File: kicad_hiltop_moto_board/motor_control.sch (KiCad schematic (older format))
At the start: 60 parts, among them Q1 CSD18540Q5B, Q2 CSD18540Q5B, Q3 CSD18540Q5B, Q4 CSD18540Q5B, Q5 CSD18540Q5B, Q6 CSD18540Q5B, Q7 CSD18540Q5B, Q8 CSD18540Q5B, U1 DRV8704

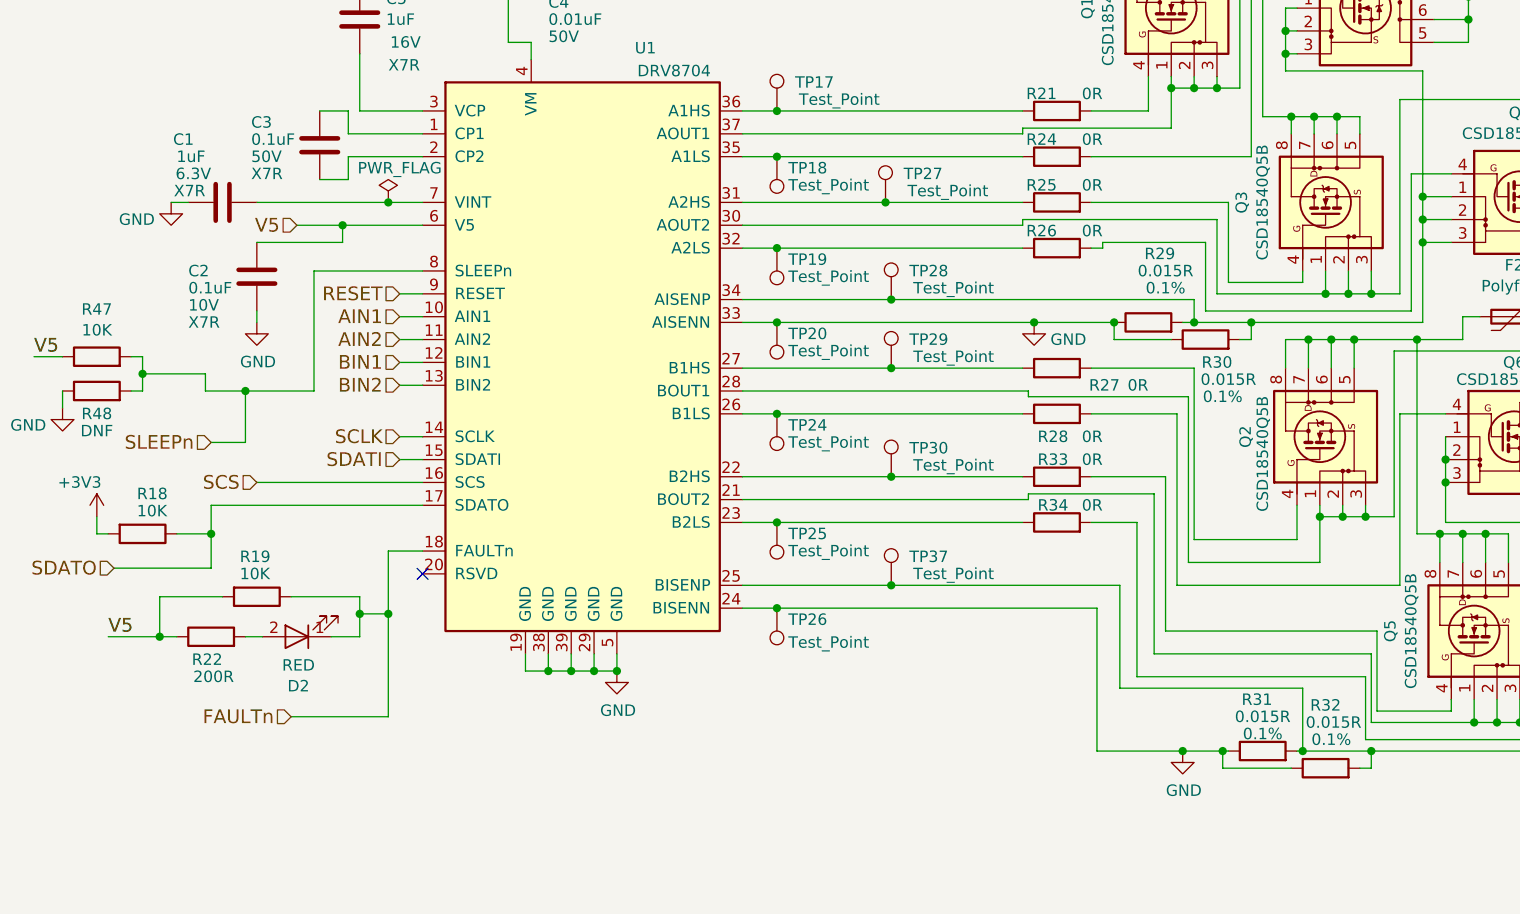
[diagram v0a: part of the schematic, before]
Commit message: added bom
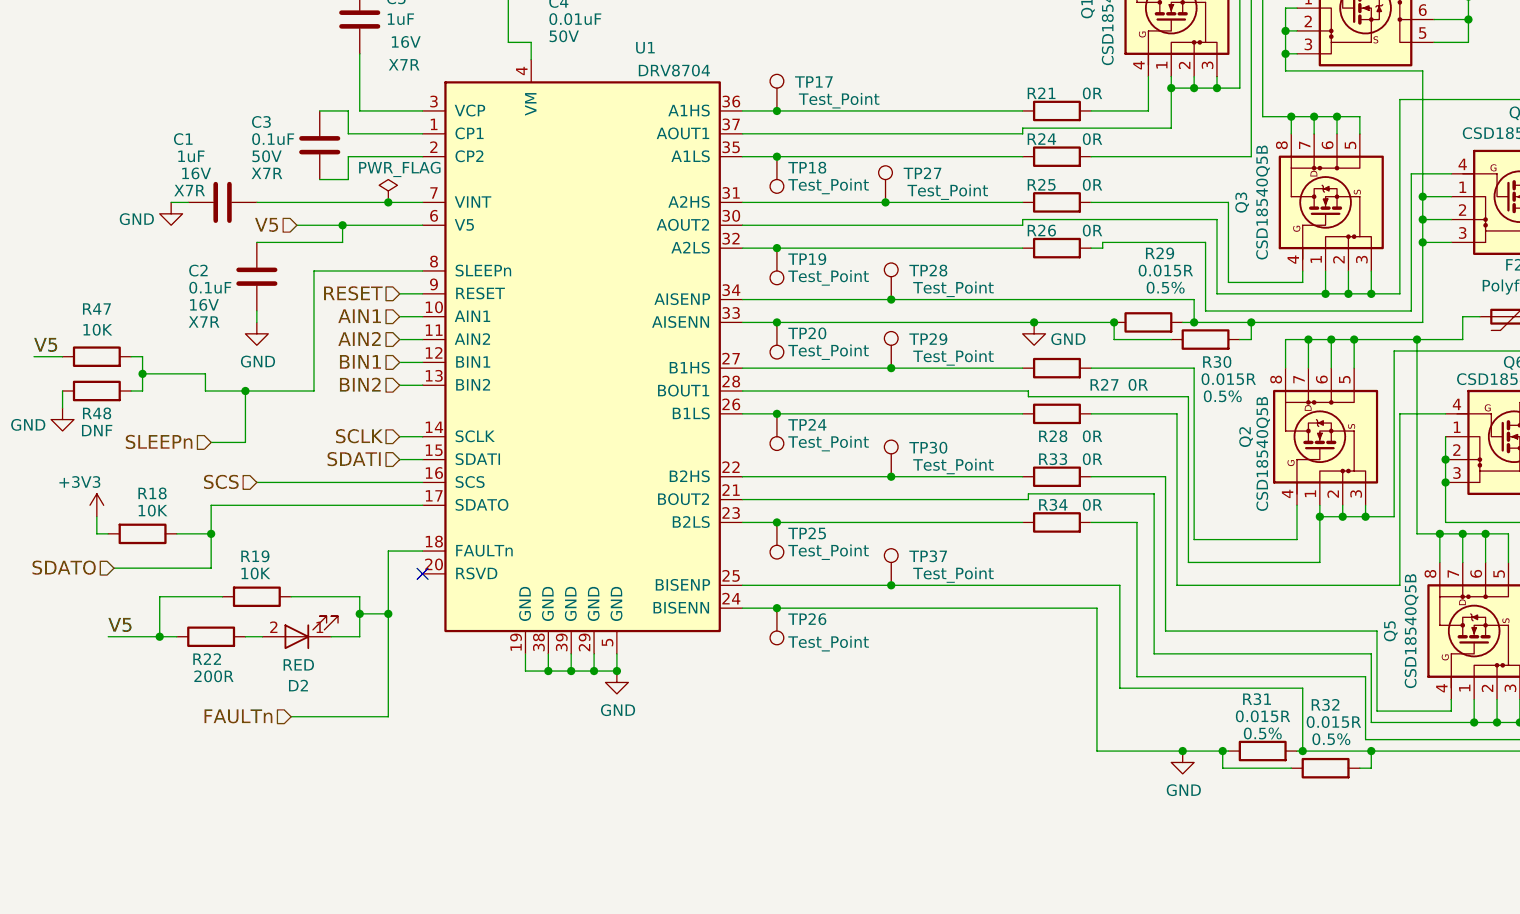
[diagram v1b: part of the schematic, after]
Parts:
- C1: Devtank (none) -> 105-014; Voltage 6.3V -> 16V
- C14, C15, C16, C17, C18, C19, C8, C9: Devtank (none) -> 108-006
- C2: Devtank (none) -> 105-019; Voltage 10V -> 16V
- C3, C6, C7: Devtank (none) -> 105-019
- C4: Devtank (none) -> 105-029
- C5: Devtank (none) -> 105-014
- D2: Devtank (none) -> 110-001
- D5: Devtank (none) -> 110-002
- F1, F2: Devtank (none) -> 190-001
- Q1, Q2, Q3, Q4, Q5, Q6, Q7, Q8: Devtank (none) -> 173-004
- R18, R19, R23, R47: Devtank (none) -> 101-010
- R21, R24, R25, R26, R27, R28, R33, R34: Devtank (none) -> 101-005
- R22: Devtank (none) -> 101-059
- R29, R30, R31, R32: Devtank (none) -> 103-006; Tolerance 0.1% -> 0.5%
- U1: Devtank (none) -> 123-012
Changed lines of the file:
@@
 F 2 "Devtank_PCB_Lib:DRV8704" H 5125 2250 50  0001 C CNN
 F 3 "http://www.ti.com/lit/ds/slvsc40f/slvsc40f.pdf" H 5125 3500 50  0001 C CNN
+F 4 "123-012" H 5125 3500 50  0001 C CNN "Devtank"
 	1    5125 3500
 	1    0    0    -1
@@
 F 2 "Devtank_PCB_Lib:TI_CSD18540Q5B" H 7750 2025 50  0001 C CIN
 F 3 "http://www.ti.com/lit/gpn/csd18540q5b" H 7700 2025 50  0001 L CNN
+F 4 "173-004" H 7750 1975 50  0001 C CNN "Devtank"
 	1    7750 1975
 	0    -1   -1   0
@@
 F 2 "Devtank_PCB_Lib:TI_CSD18540Q5B" H 8550 2075 50  0001 C CIN
 F 3 "http://www.ti.com/lit/gpn/csd18540q5b" H 8500 2075 50  0001 L CNN
+F 4 "173-004" H 8550 2025 50  0001 C CNN "Devtank"
 	1    8550 2025
 	1    0    0    -1
@@
 F 2 "Resistor_SMD:R_0603_1608Metric" V 7130 2425 50  0001 C CNN
 F 3 "" H 7200 2425 50  0001 C CNN
+F 4 "101-005" H 7200 2425 50  0001 C CNN "Devtank"
 	1    7200 2425
 	0    -1   -1   0
@@
 F 2 "Resistor_SMD:R_2512_6332Metric" V 7780 3425 50  0001 C CNN
 F 3 "" H 7850 3425 50  0001 C CNN
-F 4 "0.1%" V 7600 3350 50  0000 C CNN "Tolerance"
+F 4 "0.5%" V 7600 3350 50  0000 C CNN "Tolerance"
+F 5 "103-006" H 7850 3425 50  0001 C CNN "Devtank"
 	1    7850 3425
 	0    -1   -1   0
@@
 F 2 "Resistor_SMD:R_2512_6332Metric" V 7530 3350 50  0001 C CNN
 F 3 "" H 7600 3350 50  0001 C CNN
-F 4 "0.1%" V 7750 3275 50  0000 C CNN "Tolerance"
+F 4 "0.5%" V 7750 3275 50  0000 C CNN "Tolerance"
+F 5 "103-006" H 7600 3350 50  0001 C CNN "Devtank"
 	1    7600 3350
 	0    -1   -1   0
@@
 F 2 "Devtank_PCB_Lib:TI_CSD18540Q5B" H 8425 2875 50  0001 C CIN
 F 3 "http://www.ti.com/lit/gpn/csd18540q5b" H 8375 2875 50  0001 L CNN
+F 4 "173-004" H 8425 2825 50  0001 C CNN "Devtank"
 	1    8425 2825
 	0    -1   -1   0
@@
 F 2 "Devtank_PCB_Lib:TI_CSD18540Q5B" H 9225 2900 50  0001 C CIN
 F 3 "http://www.ti.com/lit/gpn/csd18540q5b" H 9175 2900 50  0001 L CNN
+F 4 "173-004" H 9225 2850 50  0001 C CNN "Devtank"
 	1    9225 2850
 	1    0    0    -1
@@
 F 2 "Devtank_PCB_Lib:TI_CSD18540Q5B" H 8400 3900 50  0001 C CIN
 F 3 "http://www.ti.com/lit/gpn/csd18540q5b" H 8350 3900 50  0001 L CNN
+F 4 "173-004" H 8400 3850 50  0001 C CNN "Devtank"
 	1    8400 3850
 	0    -1   -1   0
@@
 F 2 "Devtank_PCB_Lib:TI_CSD18540Q5B" H 9200 3950 50  0001 C CIN
 F 3 "http://www.ti.com/lit/gpn/csd18540q5b" H 9150 3950 50  0001 L CNN
+F 4 "173-004" H 9200 3900 50  0001 C CNN "Devtank"
 	1    9200 3900
 	1    0    0    -1
@@
 F 2 "Devtank_PCB_Lib:TI_CSD18540Q5B" H 9075 4750 50  0001 C CIN
 F 3 "http://www.ti.com/lit/gpn/csd18540q5b" H 9025 4750 50  0001 L CNN
+F 4 "173-004" H 9075 4700 50  0001 C CNN "Devtank"
 	1    9075 4700
 	0    -1   -1   0
@@
 F 2 "Devtank_PCB_Lib:TI_CSD18540Q5B" H 9875 4775 50  0001 C CIN
 F 3 "http://www.ti.com/lit/gpn/csd18540q5b" H 9825 4775 50  0001 L CNN
+F 4 "173-004" H 9875 4725 50  0001 C CNN "Devtank"
 	1    9875 4725
 	1    0    0    -1
@@
 F 2 "Resistor_SMD:R_2512_6332Metric" V 8305 5300 50  0001 C CNN
 F 3 "" H 8375 5300 50  0001 C CNN
-F 4 "0.1%" V 8500 5275 50  0000 C CNN "Tolerance"
+F 4 "0.5%" V 8500 5275 50  0000 C CNN "Tolerance"
+F 5 "103-006" H 8375 5300 50  0001 C CNN "Devtank"
 	1    8375 5300
 	0    -1   -1   0
@@
 F 2 "Resistor_SMD:R_2512_6332Metric" V 8030 5225 50  0001 C CNN
 F 3 "" H 8100 5225 50  0001 C CNN
-F 4 "0.1%" V 8175 5225 50  0000 C CNN "Tolerance"
+F 4 "0.5%" V 8175 5225 50  0000 C CNN "Tolerance"
+F 5 "103-006" H 8100 5225 50  0001 C CNN "Devtank"
 	1    8100 5225
 	0    -1   -1   0
@@
 F 4 "50V" V 5350 1725 50  0000 L CNN "Voltage"
 F 5 "LOW" H 5050 1800 50  0001 C CNN "ESR"
+F 6 "105-029" H 5050 1800 50  0001 C CNN "Devtank"
 	1    5050 1800
 	0    1    1    0
@@
 F 5 "X7R" H 3675 2450 50  0000 L CNN "Dielectric"
 F 6 "LOW" H 3975 2575 50  0001 C CNN "ESR"
+F 7 "105-019" H 3975 2575 50  0001 C CNN "Devtank"
 	1    3975 2575
 	1    0    0    -1
@@
 F 5 "X7R" H 4275 1825 50  0000 L CNN "Dielectric"
 F 6 "LOW" H 4150 2025 50  0001 C CNN "ESR"
+F 7 "105-014" H 4150 2025 50  0001 C CNN "Devtank"
 	1    4150 2025
 	1    0    0    -1
@@
 F 2 "Capacitor_SMD:C_0402_1005Metric" H 3738 3000 50  0001 C CNN
 F 3 "" H 3700 3150 50  0001 C CNN
-F 4 "10V" H 3400 3025 50  0000 L CNN "Voltage"
+F 4 "16V" H 3400 3025 50  0000 L CNN "Voltage"
 F 5 "X7R" H 3400 2950 50  0000 L CNN "Dielectric"
+F 6 "105-019" H 3700 3150 50  0001 C CNN "Devtank"
 	1    3700 3150
 	1    0    0    -1
@@
 F 2 "Capacitor_SMD:C_0603_1608Metric" H 3588 2675 50  0001 C CNN
 F 3 "" H 3550 2825 50  0001 C CNN
-F 4 "6.3V" V 3675 2875 50  0000 L CNN "Voltage"
+F 4 "16V" V 3675 2875 50  0000 L CNN "Voltage"
 F 5 "X7R" V 3600 2900 50  0000 L CNN "Dielectric"
+F 6 "105-014" H 3550 2825 50  0001 C CNN "Devtank"
 	1    3550 2825
 	0    -1   -1   0
@@
 F 2 "Resistor_SMD:R_0603_1608Metric" V 3630 4550 50  0001 C CNN
 F 3 "" H 3700 4550 50  0001 C CNN
+F 4 "101-010" H 3700 4550 50  0001 C CNN "Devtank"
 	1    3700 4550
 	0    1    1    0
@@
 F 2 "Resistor_SMD:R_0603_1608Metric" V 3130 4275 50  0001 C CNN
 F 3 "" H 3200 4275 50  0001 C CNN
+F 4 "101-010" H 3200 4275 50  0001 C CNN "Devtank"
 	1    3200 4275
 	0    1    1    0
@@
 F 3 "" H 2150 6375 50  0001 C CNN
 F 4 "50V" H 2265 6284 50  0000 L CNN "Voltage"
+F 5 "105-019" H 2150 6375 50  0001 C CNN "Devtank"
 	1    2150 6375
 	1    0    0    -1
@@
 F 3 "" H 3075 6375 50  0001 C CNN
 F 4 "50V" H 3193 6284 50  0000 L CNN "Voltage"
+F 5 "108-006" H 3075 6375 50  0001 C CNN "Devtank"
 	1    3075 6375
 	1    0    0    -1
@@
 F 3 "" H 2600 6375 50  0001 C CNN
 F 4 "50V" H 2718 6284 50  0000 L CNN "Voltage"
+F 5 "108-006" H 2600 6375 50  0001 C CNN "Devtank"
 	1    2600 6375
 	1    0    0    -1
@@
 F 3 "" H 4025 6375 50  0001 C CNN
 F 4 "50V" H 4143 6284 50  0000 L CNN "Voltage"
+F 5 "108-006" H 4025 6375 50  0001 C CNN "Devtank"
 	1    4025 6375
 	1    0    0    -1
@@
 F 3 "" H 3550 6375 50  0001 C CNN
 F 4 "50V" H 3668 6284 50  0000 L CNN "Voltage"
+F 5 "108-006" H 3550 6375 50  0001 C CNN "Devtank"
 	1    3550 6375
 	1    0    0    -1
@@
 F 3 "" H 2150 7225 50  0001 C CNN
 F 4 "50V" H 2265 7134 50  0000 L CNN "Voltage"
+F 5 "105-019" H 2150 7225 50  0001 C CNN "Devtank"
 	1    2150 7225
 	1    0    0    -1
@@
 F 3 "" H 3075 7225 50  0001 C CNN
 F 4 "50V" H 3193 7134 50  0000 L CNN "Voltage"
+F 5 "108-006" H 3075 7225 50  0001 C CNN "Devtank"
 	1    3075 7225
 	1    0    0    -1
@@
 F 3 "" H 2600 7225 50  0001 C CNN
 F 4 "50V" H 2718 7134 50  0000 L CNN "Voltage"
+F 5 "108-006" H 2600 7225 50  0001 C CNN "Devtank"
 	1    2600 7225
 	1    0    0    -1
@@
 F 3 "" H 4025 7225 50  0001 C CNN
 F 4 "50V" H 4143 7134 50  0000 L CNN "Voltage"
+F 5 "108-006" H 4025 7225 50  0001 C CNN "Devtank"
 	1    4025 7225
 	1    0    0    -1
@@
 F 3 "" H 3550 7225 50  0001 C CNN
 F 4 "50V" H 3668 7134 50  0000 L CNN "Voltage"
+F 5 "108-006" H 3550 7225 50  0001 C CNN "Devtank"
 	1    3550 7225
 	1    0    0    -1
@@
 F 2 "Fuse:Fuse_Bourns_MF-RHT200" H 8150 1125 50  0001 L CNN
 F 3 "" H 8100 1325 50  0001 C CNN
+F 4 "190-001" H 8100 1325 50  0001 C CNN "Devtank"
 	1    8100 1325
 	-1   0    0    1
@@
 F 2 "Fuse:Fuse_Bourns_MF-RHT200" H 9250 3125 50  0001 L CNN
 F 3 "" H 9200 3325 50  0001 C CNN
+F 4 "190-001" H 9200 3325 50  0001 C CNN "Devtank"
 	1    9200 3325
 	0    1    1    0
@@
 F 2 "Resistor_SMD:R_0603_1608Metric" V 3430 4725 50  0001 C CNN
 F 3 "" H 3500 4725 50  0001 C CNN
+F 4 "101-059" H 3500 4725 50  0001 C CNN "Devtank"
 	1    3500 4725
 	0    -1   -1   0
@@
 F 2 "LED_SMD:LED_0603_1608Metric" H 3875 4725 50  0001 C CNN
 F 3 "~" H 3875 4725 50  0001 C CNN
+F 4 "110-001" H 3875 4725 50  0001 C CNN "Devtank"
 	1    3875 4725
 	-1   0    0    1
@@
 F 2 "Resistor_SMD:R_0603_1608Metric" V 7130 2625 50  0001 C CNN
 F 3 "" H 7200 2625 50  0001 C CNN
+F 4 "101-005" H 7200 2625 50  0001 C CNN "Devtank"
 	1    7200 2625
 	0    -1   -1   0
@@
 F 2 "Resistor_SMD:R_0603_1608Metric" V 7130 2825 50  0001 C CNN
 F 3 "" H 7200 2825 50  0001 C CNN
+F 4 "101-005" H 7200 2825 50  0001 C CNN "Devtank"
 	1    7200 2825
 	0    -1   -1   0
@@
 F 2 "Resistor_SMD:R_0603_1608Metric" V 7130 3025 50  0001 C CNN
 F 3 "" H 7200 3025 50  0001 C CNN
+F 4 "101-005" H 7200 3025 50  0001 C CNN "Devtank"
 	1    7200 3025
 	0    -1   -1   0
@@
 F 2 "Resistor_SMD:R_0603_1608Metric" V 7130 3550 50  0001 C CNN
 F 3 "" H 7200 3550 50  0001 C CNN
+F 4 "101-005" H 7200 3550 50  0001 C CNN "Devtank"
 	1    7200 3550
 	0    -1   -1   0
@@
 F 2 "Resistor_SMD:R_0603_1608Metric" V 7130 3750 50  0001 C CNN
 F 3 "" H 7200 3750 50  0001 C CNN
+F 4 "101-005" H 7200 3750 50  0001 C CNN "Devtank"
 	1    7200 3750
 	0    -1   -1   0
@@
 F 2 "Resistor_SMD:R_0603_1608Metric" V 7130 4025 50  0001 C CNN
 F 3 "" H 7200 4025 50  0001 C CNN
+F 4 "101-005" H 7200 4025 50  0001 C CNN "Devtank"
 	1    7200 4025
 	0    -1   -1   0
@@
 F 2 "Resistor_SMD:R_0603_1608Metric" V 7130 4225 50  0001 C CNN
 F 3 "" H 7200 4225 50  0001 C CNN
+F 4 "101-005" H 7200 4225 50  0001 C CNN "Devtank"
 	1    7200 4225
 	0    -1   -1   0
@@
 F 2 "Resistor_SMD:R_0603_1608Metric" V 2930 3500 50  0001 C CNN
 F 3 "" H 3000 3500 50  0001 C CNN
+F 4 "101-010" H 3000 3500 50  0001 C CNN "Devtank"
 	1    3000 3500
 	0    -1   -1   0
@@
 F 2 "LED_SMD:LED_0603_1608Metric" H 1050 1700 50  0001 C CNN
 F 3 "~" H 1050 1700 50  0001 C CNN
+F 4 "110-002" H 1050 1700 50  0001 C CNN "Devtank"
 	1    1050 1700
 	0    -1   -1   0
@@
 F 2 "Resistor_SMD:R_0603_1608Metric" V 980 1350 50  0001 C CNN
 F 3 "" H 1050 1350 50  0001 C CNN
+F 4 "101-010" H 1050 1350 50  0001 C CNN "Devtank"
 	1    1050 1350
 	1    0    0    -1
